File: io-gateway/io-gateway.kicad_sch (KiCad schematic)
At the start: 8 parts, among them J1 1752201, J2 1752201, J3 1752201, J4 Screw_Terminal_01x09, J5 Screw_Terminal_01x09, J6 Screw_Terminal_01x09

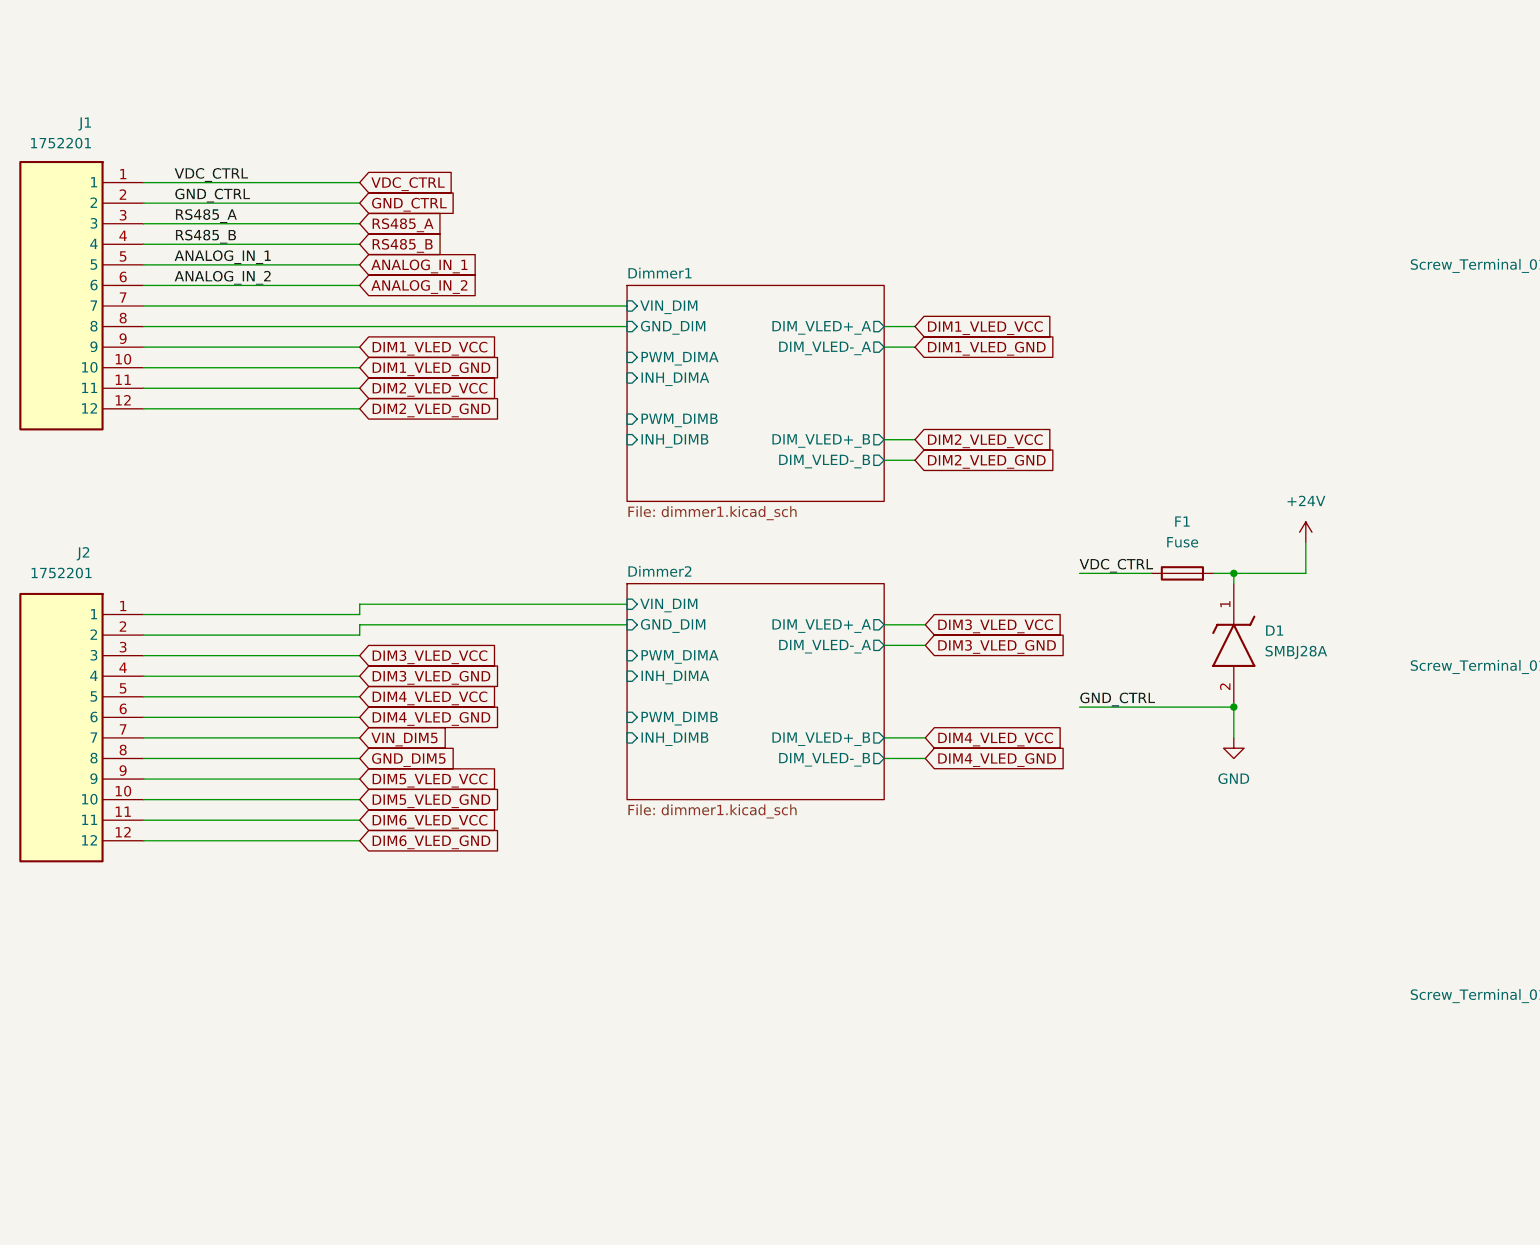
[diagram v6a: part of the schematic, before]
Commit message: fix some drc issues
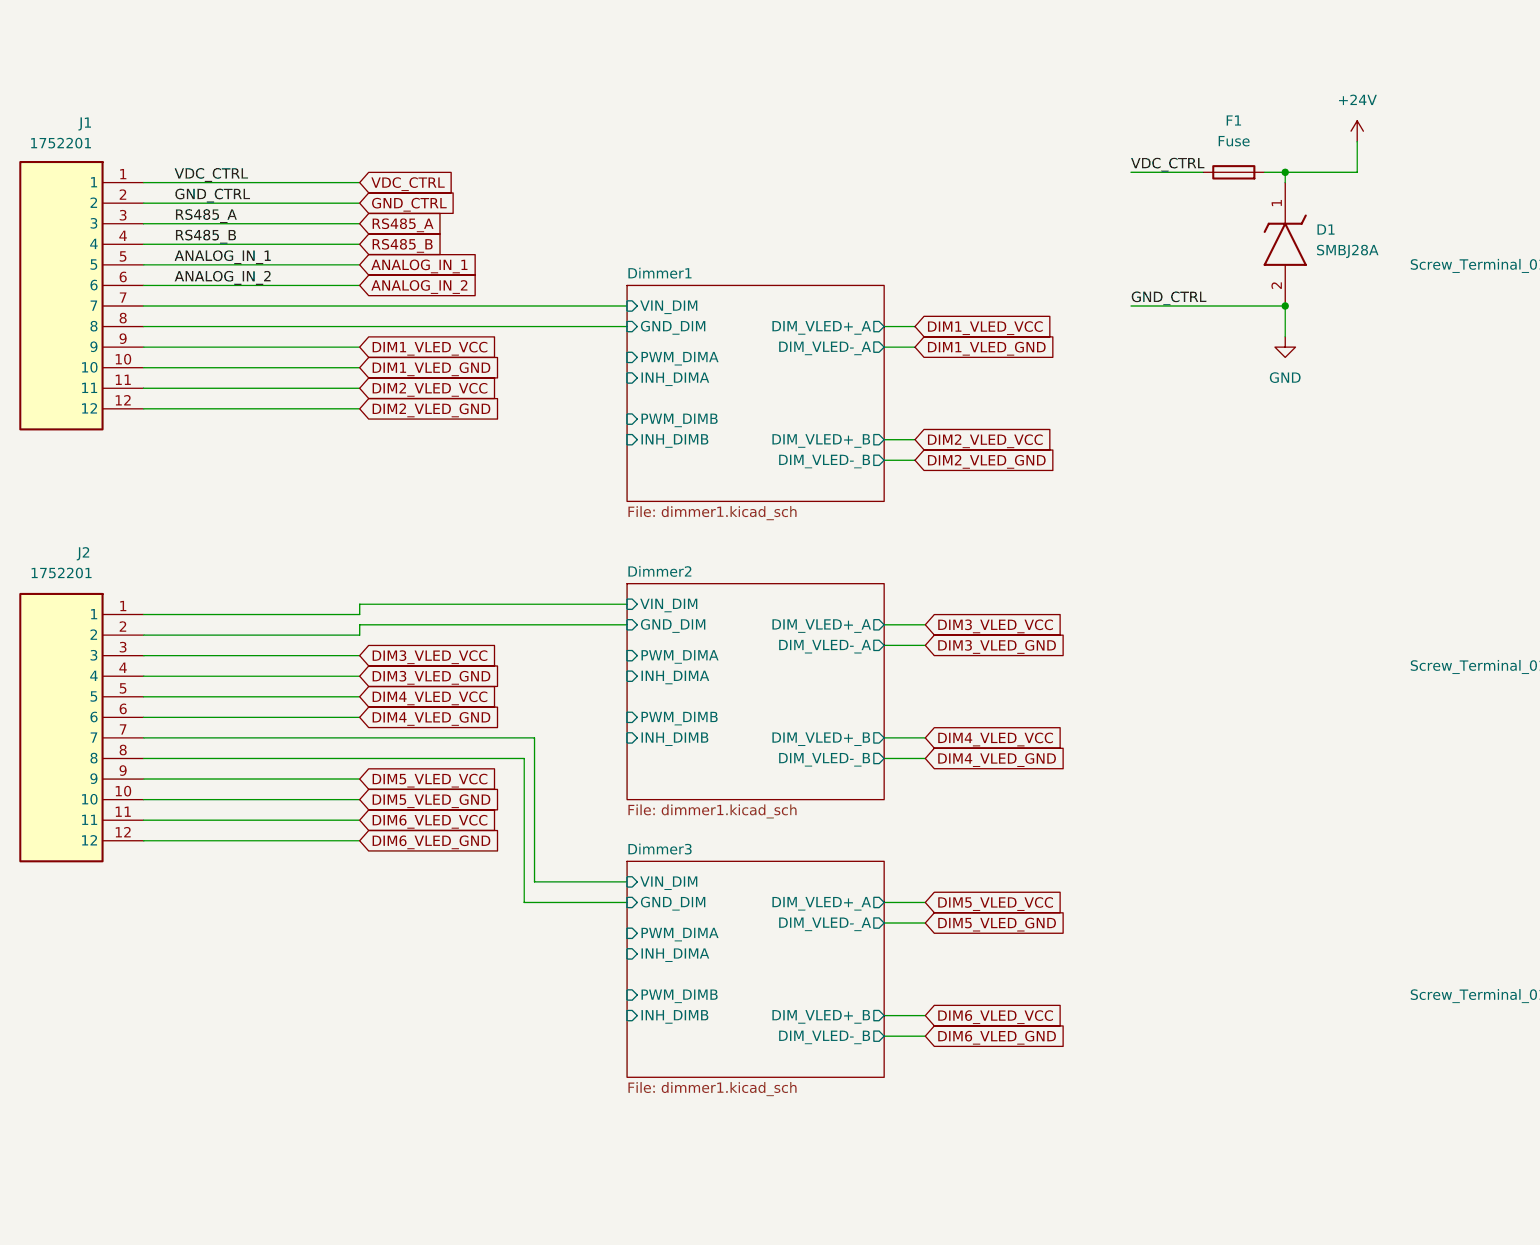
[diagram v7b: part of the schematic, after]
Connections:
- net GND_DIM5: no longer J2.8
- net VIN_DIM5: no longer J2.7
- new net Dimmer3/GND_DIM: J2.8
- new net Dimmer3/VIN_DIM: J2.7
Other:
- added sheet Dimmer3 (dimmer1.kicad_sch)
- moved on the sheet: D1, F1

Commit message: upd
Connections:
- net GND_DIM3 renamed Dimmer4/GND_DIM
- net VIN_DIM3 renamed Dimmer4/VIN_DIM
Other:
- added sheet Dimmer4 (dimmer1.kicad_sch)
- moved on the sheet: J3
